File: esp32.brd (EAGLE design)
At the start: 91.4 x 79.7 mm, 66 parts, among them IC1 PEC11R-4230K-S00243D, IC2 AD8532ARZ, IC3 LM1117MP-3.3_NOPBSMD, T1 BST82-1, T2 BST82-1, T3 BST82-1, U1 ESP32-WROOM-32D, X1 JST-XH-02-PIN-LONG-PAD, X2 JST-XH-03-PIN-LONG-PAD, X3 JST-XH-03-PIN-LONG-PAD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

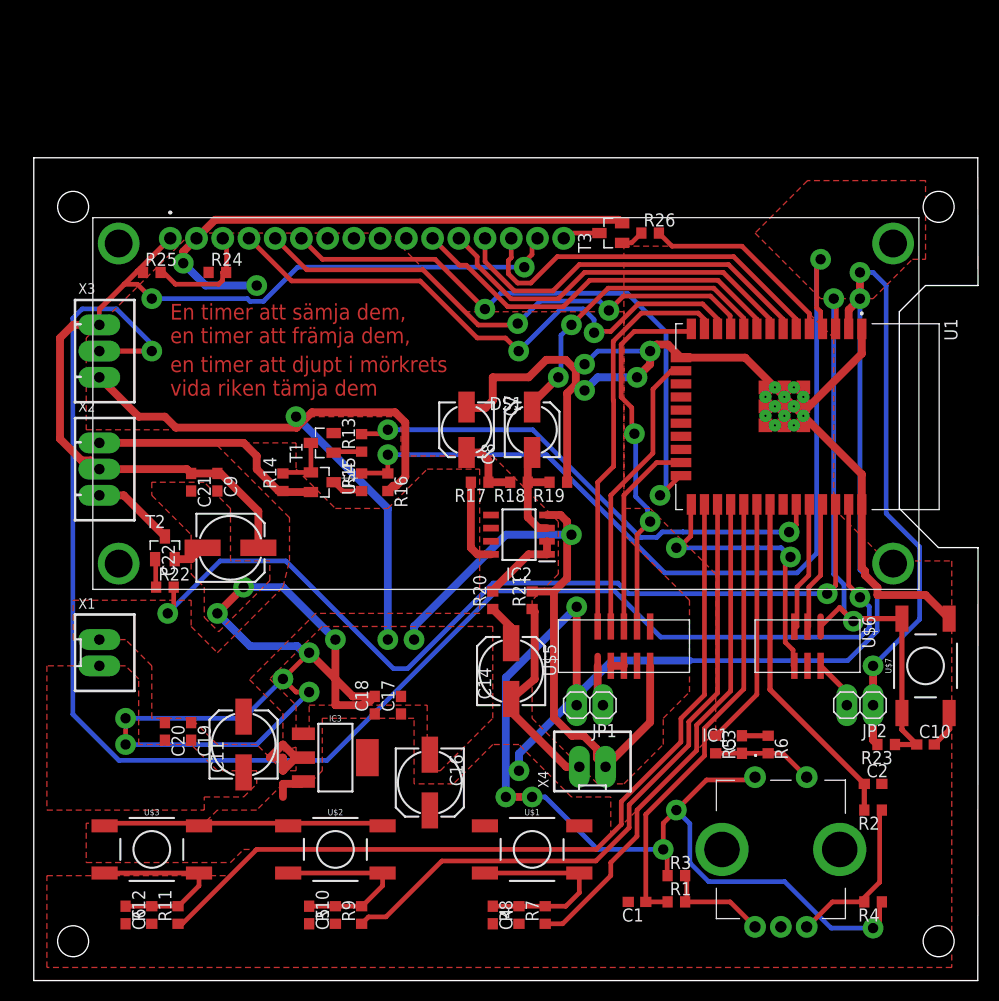
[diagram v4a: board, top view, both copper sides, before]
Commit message: Delad upp jordplanet till flera beroende på signal, hört att det ska vara bra att ta bort loopar i jorden.
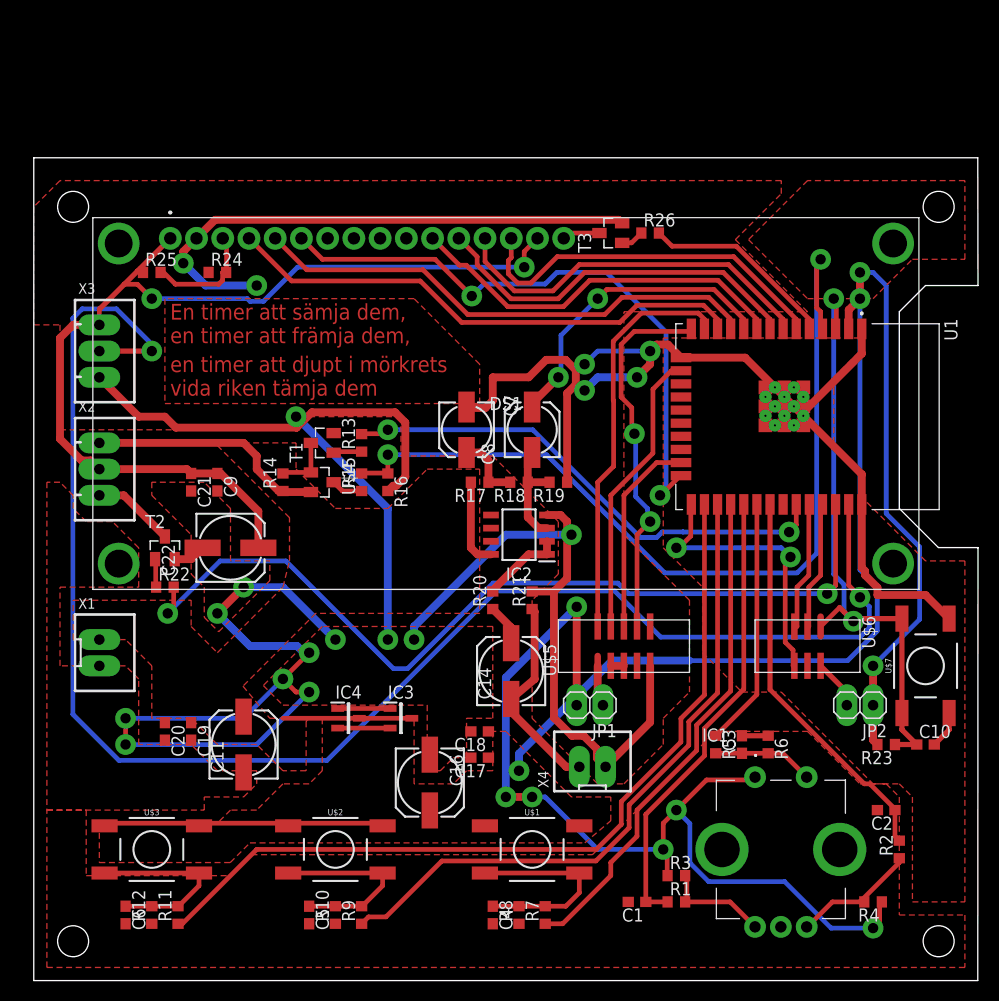
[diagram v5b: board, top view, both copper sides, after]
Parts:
- added IC4: MCP1700T-3302E_TT, Test:SOT95P237X112-3N
- IC3: value LM1117MP-3.3_NOPBSMD -> MCP1700T-3302E_TT; device Test:SOT223 -> Test:SOT95P237X112-3N
- moved C18 10.5 mm to (43.2, 24.1), turned to 180 degrees
- moved C17 9.16 mm to (43.2, 21.6), turned to 180 degrees
- moved IC3 7.41 mm to (35.6, 25.4), turned to 0 degrees
- moved R2 4.58 mm to (83.8, 12.7), turned to 90 degrees
- moved C2 2.84 mm to (82.5, 16.5), turned to 180 degrees
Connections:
- net +3V3: now also IC3.2, IC4.2; no longer IC3.3, IC3.4
- net GND: now also IC4.1
- net VCC: now also IC3.3, IC4.3; no longer IC3.2
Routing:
- net GND: track 381.7 -> 368.2 mm
- net LCD_RS: track 56.1 -> 50.9 mm, vias 2 -> 0
- net ROT_ENC_B: track 33.4 -> 38.1 mm
- net N$2: track 16.4 -> 12.4 mm
- net VCC: track 40.4 -> 44.2 mm
- net LCD_RW: track 51.6 -> 49.7 mm, vias 2 -> 0
- net +3V3: track 255.3 -> 257.0 mm
- net LCD_E: track 59.2 -> 59.8 mm

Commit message: Nya upplägget fungera bra, kanske till och med mindre vior än innan, får in mer på mindre plats också. Kommit kanske 70% nu.
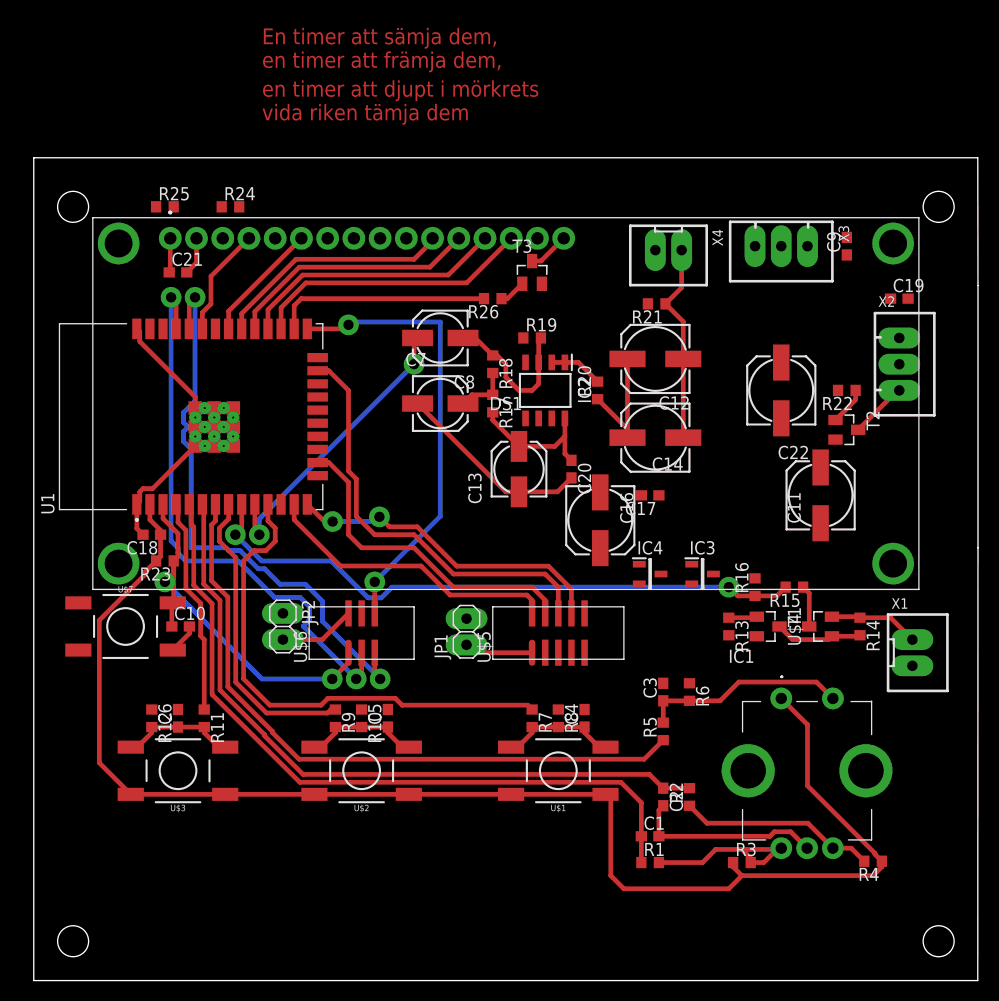
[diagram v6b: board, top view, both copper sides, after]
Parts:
- added C12: 270uF, rcl:153CLV-0605
- added C13: (no value), rcl:153CLV-0505
- moved C19 80.4 mm to (83.8, 66.0), turned to 0 degrees
- moved X1 78.7 mm to (85.1, 31.8)
- moved X2 78.1 mm to (83.8, 59.7)
- moved U$7 77.6 mm to (8.89, 34.3), turned to 0 degrees
- moved C10 73.0 mm to (14.2, 34.3)
- moved R23 72.1 mm to (12.7, 40.6)
- moved R22 68.7 mm to (78.7, 57.1), turned to 180 degrees
- moved T2 67.0 mm to (78.7, 53.3), turned to 270 degrees
- moved X3 66.8 mm to (72.4, 71.1), turned to 180 degrees
- moved C9 65.1 mm to (78.7, 71.1), turned to 90 degrees
- moved C11 60.9 mm to (76.2, 47.0)
- moved U1 59.7 mm to (15.2, 54.6), turned to 90 degrees
- moved R14 57.6 mm to (80.0, 34.3), turned to 270 degrees
- moved JP2 56.4 mm to (24.1, 34.3), turned to 270 degrees
- moved C22 55.5 mm to (72.4, 57.1), turned to 90 degrees
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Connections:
- net BAT_MONITOR_ANALOG: now also U1.9; no longer U1.4
- net BAT_MONITOR_ENABLE: no longer U1.33
- net BTN_1: now also U1.11; no longer U1.28
- net BTN_2: now also U1.8; no longer U1.27
- net BTN_3: now also U1.4; no longer U1.26
- net ENABLE_5V: no longer U1.36
- net ESP_EN: no longer U$7.P$1
- net GND: now also C13.-
- net LCD_D4: now also U1.30; no longer U1.9
- net LCD_D5: now also U1.29; no longer U1.8
- net LCD_D6: now also U1.28; no longer U1.7
- net LCD_D7: now also U1.27; no longer U1.6
- net LCD_DIMMER: now also U1.26; no longer U1.5
- net LCD_E: now also U1.31; no longer U1.24
- net LCD_RS: now also U1.33; no longer U1.12
- net LCD_RW: no longer U1.11
- net N$14: now also C12.+
- net ROT_ENC_A: now also U1.5; no longer U1.29
- net ROT_ENC_B: now also U1.6; no longer U1.31
- net ROT_ENC_BTN: now also U1.7; no longer U1.30
- net SPEAKER_OUT: now also C12.-
- net VCC: now also C13.+
- net WS2812B_DATA: no longer U1.37
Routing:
- net GND: track 368.2 -> 65.7 mm, vias 18 -> 0
- net WS2812B_DATA: track 154.3 -> 0.00 mm, vias 2 -> 0
- net +3V3: track 257.0 -> 135.9 mm, vias 10 -> 0
- net +5V: track 95.7 -> 3.34 mm, vias 2 -> 0
- net ENABLE_5V: track 85.9 -> 0.00 mm, vias 2 -> 0
- net BTN_3: track 81.2 -> 21.0 mm
- net LCD_RW: track 49.7 -> 0.00 mm
- net BAT_MONITOR_ENABLE: track 49.1 -> 0.00 mm, vias 2 -> 0
- net LCD_E: track 59.8 -> 11.7 mm, vias 2 -> 0
- net ESP_RX: track 12.6 -> 56.1 mm, vias 0 -> 2
- net ESP_TX: track 12.6 -> 55.3 mm, vias 0 -> 2
- net ROT_ENC_BTN: track 24.1 -> 64.4 mm
- net LCD_RS: track 50.9 -> 10.6 mm
- net BTN_2: track 64.6 -> 29.3 mm
- net ROT_ENC_B: track 38.1 -> 68.2 mm
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- removed copper zone on layer 1, net +3V3
- removed copper zone on layer 1, net GND
- removed copper zone on layer 1, net VCC
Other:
- outline, holes or cut-outs redrawn

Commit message: All är routat, behövs dock nya avtryck för JST och skämen.
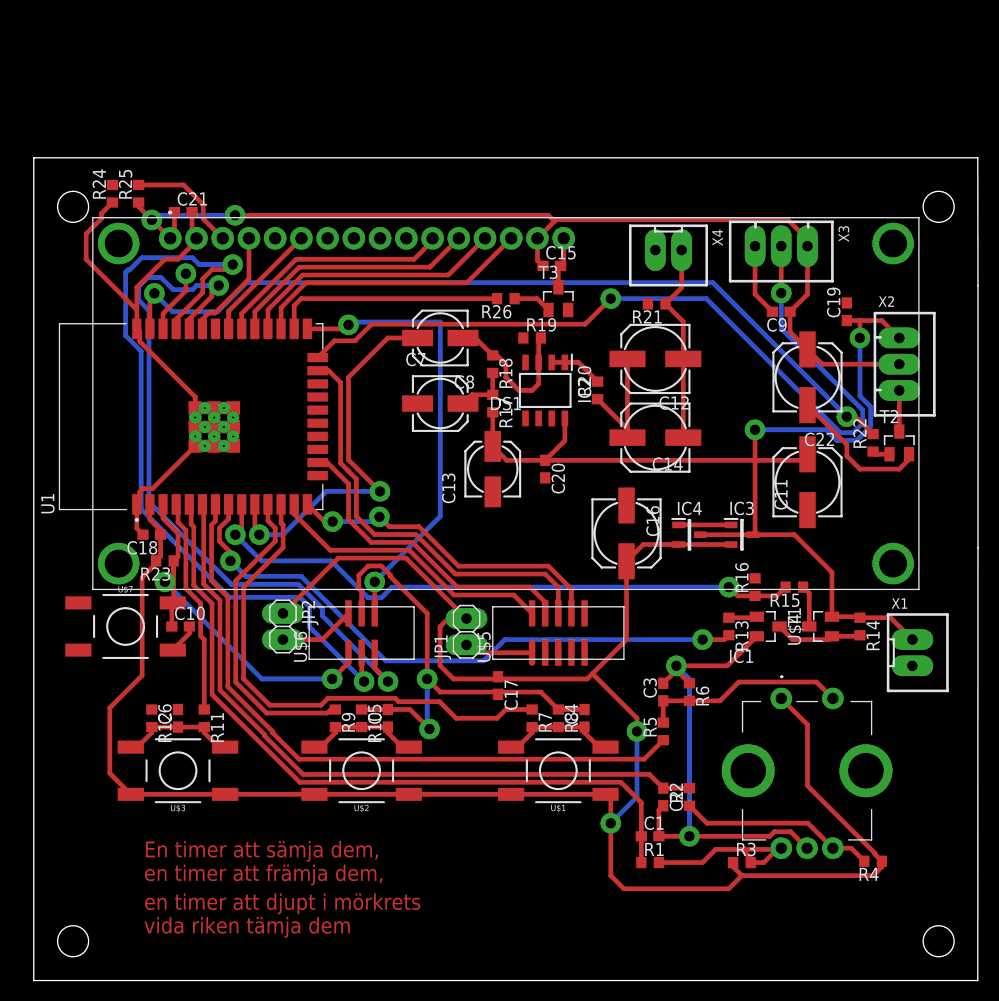
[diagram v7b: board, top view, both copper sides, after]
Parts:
- added C15: 0.1uF, rcl:C0603
- moved C17 23.6 mm to (45.0, 28.6), turned to 270 degrees
- moved R24 11.5 mm to (7.62, 76.2), turned to 90 degrees
- moved C9 8.98 mm to (72.4, 64.8), turned to 180 degrees
- moved C21 5.86 mm to (14.5, 74.4)
- moved R22 5.68 mm to (81.3, 52.1), turned to 90 degrees
- moved IC3 5.39 mm to (68.6, 43.2)
- moved IC4 5.39 mm to (63.5, 43.2)
- moved C19 5.24 mm to (78.7, 64.8), turned to 90 degrees
- moved T2 5.24 mm to (83.8, 52.1), turned to 0 degrees
- moved T3 3.59 mm to (50.8, 66.0)
- moved C22 2.84 mm to (74.9, 58.4)
- moved C16 2.84 mm to (57.4, 43.3)
- moved R25 2.84 mm to (10.2, 76.2), turned to 90 degrees
- moved C13 2.54 mm to (44.5, 49.5)
- moved C20 2.54 mm to (49.5, 49.5)
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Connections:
- new net SPARE_GPIO: U1.36
- net +5V: now also C15.1
- net BAT_MONITOR_ENABLE: now also U1.8
- net BTN_1: now also U1.12; no longer U1.11
- net BTN_2: now also U1.11; no longer U1.8
- net ENABLE_5V: now also U1.37
- net N$18: now also C15.2
- net WS2812B_DATA: now also U1.24
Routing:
- net GND: track 65.7 -> 175.1 mm, vias 0 -> 4
- net +5V: track 3.34 -> 99.0 mm, vias 0 -> 2
- net +3V3: track 135.9 -> 220.2 mm, vias 0 -> 2
- net VCC: track 22.2 -> 105.6 mm, vias 0 -> 2
- net ENABLE_5V: track 0.00 -> 81.4 mm, vias 0 -> 2
- net WS2812B_DATA: track 0.00 -> 81.3 mm, vias 0 -> 2
- net BAT_MONITOR_ENABLE: track 0.00 -> 59.6 mm, vias 0 -> 2
- net ESP_TX: track 55.3 -> 76.7 mm
- net ESP_RX: track 56.1 -> 69.5 mm
- net N$17: track 0.00 -> 11.1 mm
- net AUDIO_FROM_ESP32: track 28.5 -> 37.1 mm
- net SPARE_GPIO: track 0.00 -> 6.26 mm, vias 0 -> 1
- net N$11: track 3.67 -> 1.69 mm
- net N$15: track 5.56 -> 3.98 mm
- net LCD_DIMMER: track 20.9 -> 22.2 mm
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
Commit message: Tror fan att den är färdig nu, allt som ska bli SMT är SMT nu och rätt pinnar för rätt sak förhoppningsvis.
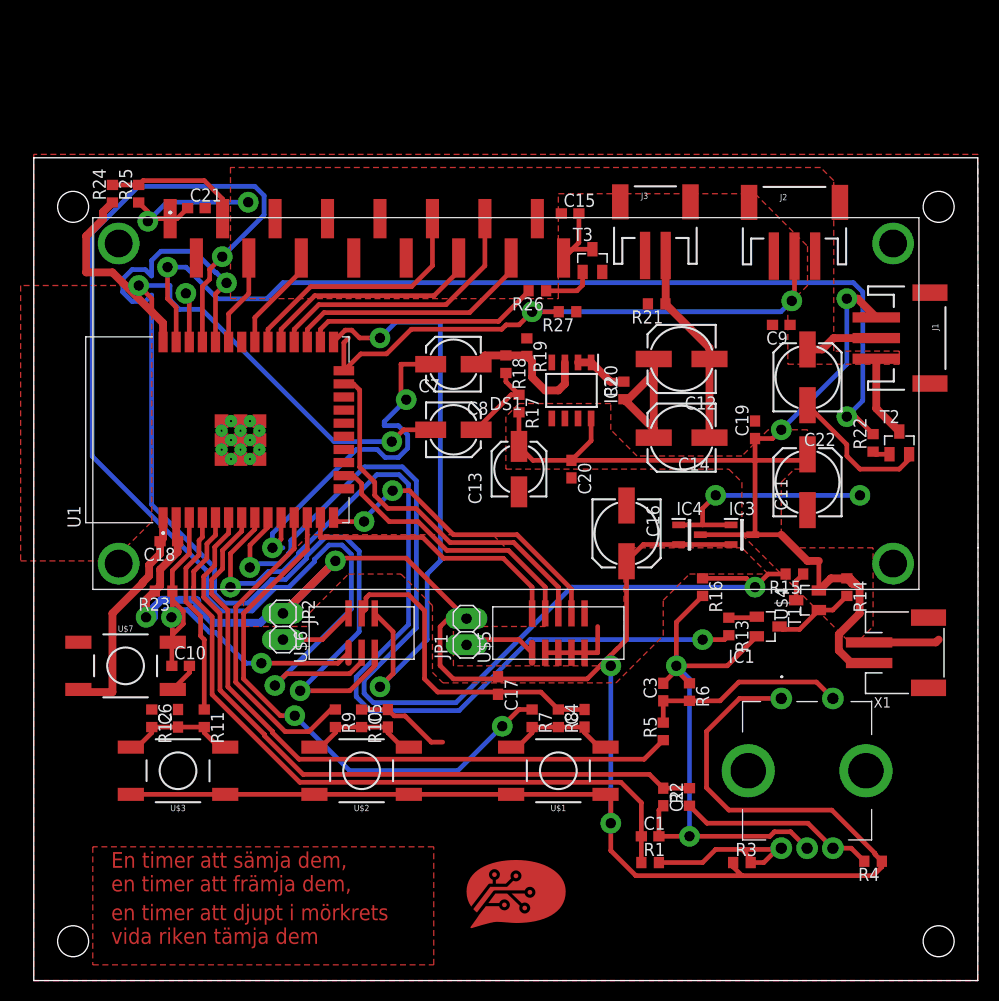
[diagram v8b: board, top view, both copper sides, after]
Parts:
- removed X2, X3: JST-XH-03-PIN-LONG-PAD, Rembrandt Electronics - JST XH Connectors v1-0:JST-XH-03-PACKAGE-LONG-PAD
- removed X4: JST-XH-02-PIN-LONG-PAD, Rembrandt Electronics - JST XH Connectors v1-0:JST-XH-02-PACKAGE-LONG-PAD
- added J1, J2: 3-PIN SMD, SparkFun-Connectors:JST-3-SMD
- added J3: (no value), SparkFun-Connectors:JST-2-SMD
- added R27: 100, rcl:R0603
- added U$8: TOUCHMARK, Test:TOUCHMARK
- DS1: device Test:NHD0216XZFSWGBW_DUPONTCONNECTOR -> Test:NHD0216XZFSWGBW_SMT
- X1: value JST-XH-02-PIN-LONG-PAD -> S2B-PH-SM4-TB; device Rembrandt Electronics - JST XH Connectors v1-0:JST-XH-02-PACKAGE-LONG-PAD -> con-JST PH:S2B-PH-SM4-TB
- moved C19 14.5 mm to (69.8, 53.3)
- moved C15 5.38 mm to (51.9, 74.3)
- moved R16 5.08 mm to (64.8, 38.1), turned to 270 degrees
- moved T3 4.95 mm to (54.1, 69.7)
- moved X1 4.19 mm to (80.9, 31.8)
- moved R14 4.02 mm to (78.7, 38.1)
- moved C10 3.81 mm to (14.2, 30.5)
- moved U$7 3.81 mm to (8.89, 30.5)
- moved R26 3.14 mm to (48.8, 66.8)
- moved R23 2.92 mm to (12.6, 37.7)
- moved C7 2.84 mm to (40.6, 53.3)
- moved C8 2.84 mm to (40.6, 59.7)
- moved U1 2.84 mm to (17.8, 53.3)
- moved U$4 2.84 mm to (74.9, 36.8)
- moved C12 2.54 mm to (62.7, 60.2)
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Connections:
- net +5V: now also DS1.P$1, DS1.P$15, J1.2, J2.3; no longer DS1.1, DS1.15, X2.2, X3.1
- net GND: now also DS1.P$2, J2.1, J3.1, R27.1; no longer DS1.2, X3.3, X4.2
- net LCD_D4: now also DS1.P$11; no longer DS1.11
- net LCD_D5: now also DS1.P$12; no longer DS1.12
- net LCD_D6: now also DS1.P$13; no longer DS1.13
- net LCD_D7: now also DS1.P$14; no longer DS1.14
- net LCD_E: now also DS1.P$6; no longer DS1.6
- net LCD_RS: now also DS1.P$4; no longer DS1.4
- net LCD_RW: now also DS1.P$5; no longer DS1.5
- net N$15: now also J1.3; no longer X2.3
- net N$17: now also DS1.P$3; no longer DS1.3
- net N$18: now also DS1.P$16; no longer DS1.16
- net SPEAKER_OUT: now also J3.2; no longer X4.1
- net VCC: now also J1.1; no longer X2.1
- net WS2812B_DATA: now also J2.2, R27.2; no longer X3.2
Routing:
- net +5V: track 99.0 -> 24.2 mm
- net GND: track 175.1 -> 230.9 mm, vias 4 -> 6
- net ESP_TX: track 76.7 -> 119.1 mm
- net BAT_MONITOR_ANALOG: track 60.1 -> 101.4 mm
- net BAT_MONITOR_ENABLE: track 59.6 -> 92.3 mm
- net ESP_RX: track 69.5 -> 99.2 mm
- net WS2812B_DATA: track 81.3 -> 56.6 mm
- net +3V3: track 220.2 -> 241.0 mm, vias 2 -> 4
- net ESP_IO_0: track 44.0 -> 57.9 mm
- net ENABLE_5V: track 81.4 -> 93.2 mm
- net VCC: track 105.6 -> 99.7 mm
- net N$14: track 12.5 -> 17.8 mm
- net TDO: track 41.2 -> 36.6 mm
- net N$15: track 3.98 -> 7.97 mm
- net TCK: track 30.8 -> 27.1 mm
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- added copper zone on layer 1, net +3V3
- added copper zone on layer 1, net +5V
- added copper zone on layer 1, net GND
- added copper zone on layer 1, net VCC
